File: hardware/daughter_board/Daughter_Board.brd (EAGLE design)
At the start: 65 x 30 mm, 54 parts, among them IC1 LMV358MMX, IC2 LMV358MMX, IC3 ATMEGA2560-16AU, IC5 LMV358MMX, IC8 LMV358MMX, IC9 LMV358MMX, U1 TXB0108DQSR, Y1 CSTCE16M0V53-R0 16MHZ

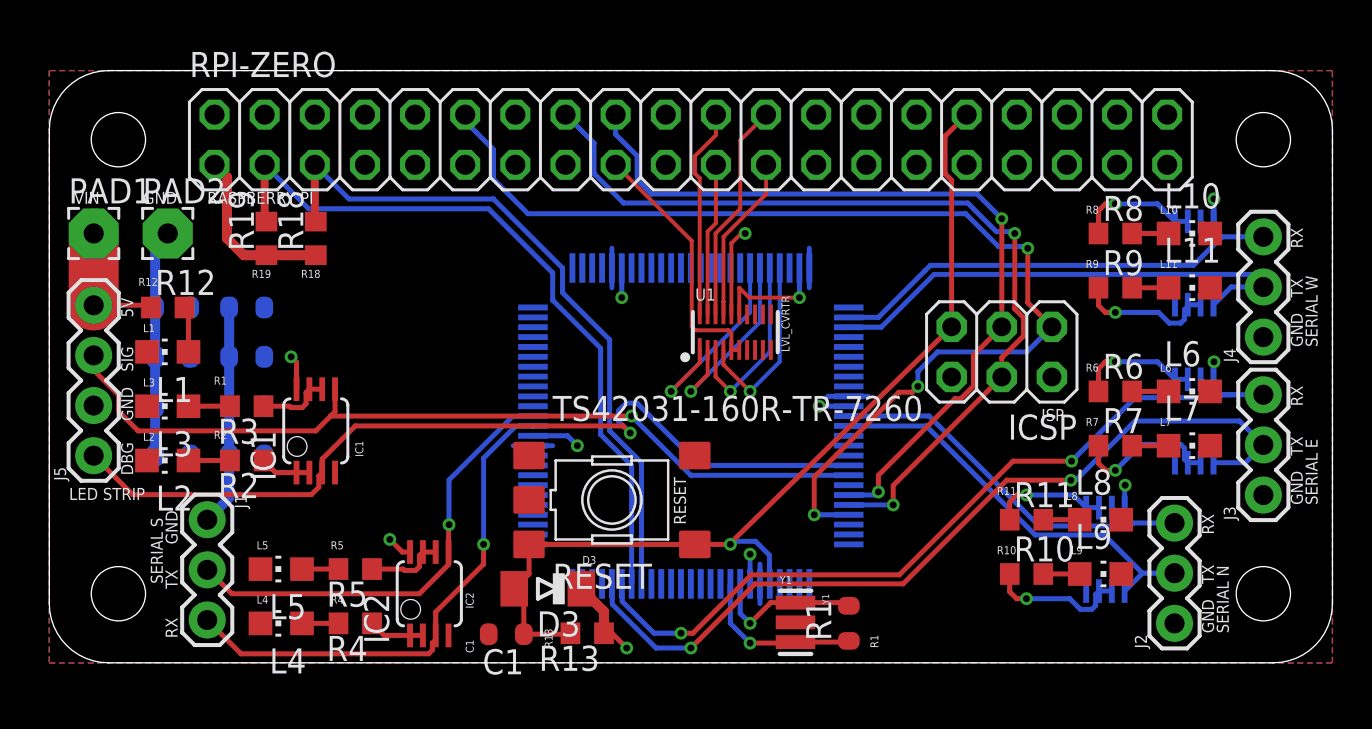
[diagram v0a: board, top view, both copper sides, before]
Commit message: fix issues generated by seeedstudio dru
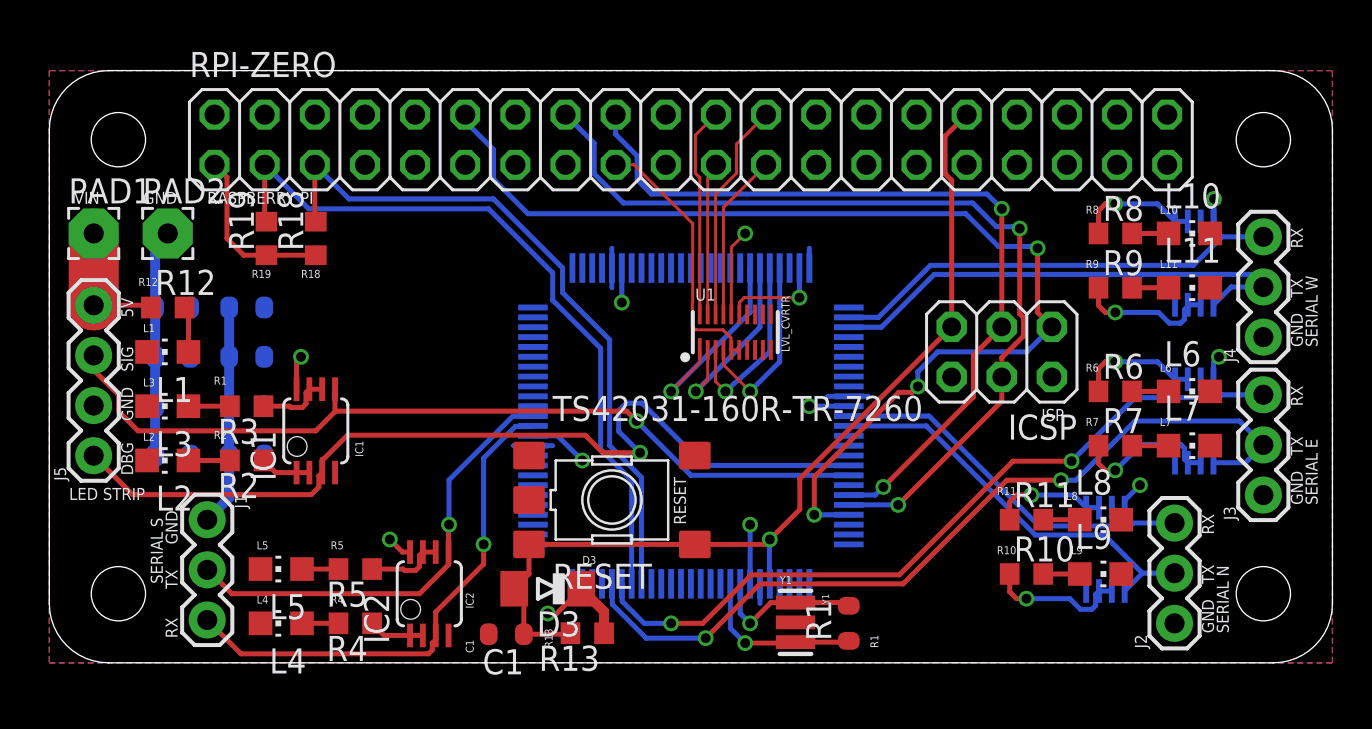
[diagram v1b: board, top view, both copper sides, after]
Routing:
- net GND: track 39.0 -> 41.6 mm
- net RXD1: track 41.5 -> 39.7 mm
- net PH5: track 44.8 -> 46.6 mm
- net +5V: track 28.4 -> 27.0 mm
- net RESET: track 48.5 -> 47.9 mm

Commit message: some DRC fixes
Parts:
- _: value TS42031-160R-TR-7260 -> (none)
- renumbered RESET to _
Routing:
- net +5V: track 27.0 -> 70.3 mm, vias 4 -> 8
- net GND: track 41.6 -> 46.3 mm
- net RESET: track 47.9 -> 49.0 mm

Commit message: export gerber files and create bom
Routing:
- net 3V3_OUT: track 22.4 -> 39.5 mm
- net +5V: track 70.3 -> 78.7 mm
- net GND: track 46.3 -> 50.2 mm
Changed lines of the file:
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@@
 <?xml version="1.0" encoding="utf-8"?>
 <!DOCTYPE eagle SYSTEM "eagle.dtd">
-<eagle version="8.3.2">
+<eagle version="8.4.0">
 <drawing>
 <settings>
@@
 <param name="dpMaxLengthDifference" value="10mm"/>
 <param name="dpGapFactor" value="2.5"/>
-<param name="checkGrid" value="0"/>
-<param name="checkAngle" value="0"/>
 <param name="checkFont" value="1"/>
 <param name="checkRestrict" value="0"/>
+<param name="checkStop" value="0"/>
 <param name="useDiameter" value="13"/>
 <param name="maxErrors" value="50"/>
@@
 <wire x1="32.5944" y1="22.25" x2="29.6144" y2="25.23" width="0.1524" layer="1"/>
 <wire x1="29.6144" y1="25.23" x2="28.69" y2="25.23" width="0.1524" layer="1"/>
-<wire x1="13.5" y1="20.65" x2="28.69" y2="25.23" width="0" layer="19" extent="1-1"/>
+<wire x1="28.69" y1="25.23" x2="24.11" y2="20.65" width="0.254" layer="1"/>
+<wire x1="24.11" y1="20.65" x2="13.5" y2="20.65" width="0.254" layer="1"/>
 </signal>
 <signal name="GPIO4">
@@
 <wire x1="9.96605625" y1="2" x2="8.52605625" y2="3.44" width="0.254" layer="1"/>
 <wire x1="8.52605625" y1="3.44" x2="7.06" y2="3.44" width="0.254" layer="1"/>
-<wire x1="5.361" y1="10.5" x2="4.95" y2="10.25" width="0" layer="19" extent="1-16"/>
+<wire x1="2.2479" y1="13.033" x2="4.95" y2="10.3309" width="0.254" layer="1"/>
+<wire x1="4.95" y1="10.3309" x2="4.95" y2="10.25" width="0.254" layer="1"/>
 </signal>
 <signal name="GPIO17">
@@
 <wire x1="34.55" y1="21.05" x2="35.25" y2="21.75" width="0.1524" layer="1"/>
 <via x="25.25" y="2.5" extent="1-16" drill="0.5"/>
-<wire x1="24.5" y1="11" x2="25.5" y2="11" width="0.3048" layer="16"/>
-<wire x1="25.5" y1="11" x2="25.75" y2="10.75" width="0.3048" layer="16"/>
 <wire x1="23.5" y1="11" x2="24.5" y2="11" width="0.3048" layer="16"/>
 <wire x1="23.5" y1="11" x2="23.25" y2="10.75" width="0.3048" layer="16"/>
@@
 <wire x1="28.5" y1="8.25" x2="31" y2="8.25" width="0.508" layer="1"/>
 <via x="31" y="8.25" extent="1-16" drill="0.5"/>
-<wire x1="36" y1="4" x2="36" y2="7.75" width="0.254" layer="16"/>
-<wire x1="25.5" y1="11" x2="25.5" y2="10.866975" width="0.254" layer="16"/>
-<wire x1="25.5" y1="10.866975" x2="25.5802" y2="10.786775" width="0.254" layer="16"/>
-<wire x1="25.5802" y1="10.786775" x2="25.5802" y2="10.6698" width="0.254" layer="16"/>
-<wire x1="25.5802" y1="10.6698" x2="26" y2="10.25" width="0.254" layer="16"/>
+<wire x1="36" y1="7.75" x2="36" y2="4" width="0.254" layer="16"/>
 <wire x1="28.5" y1="20" x2="28.5" y2="21.5" width="0.254" layer="16"/>
 <wire x1="5.15" y1="18" x2="2.3609" y2="18" width="0.508" layer="1"/>
@@
 <wire x1="48.6404" y1="3.6060625" x2="49.1439375" y2="4.1096" width="0.508" layer="16"/>
 <wire x1="58.5" y1="3.25" x2="58.397" y2="3.147" width="0.508" layer="16"/>
-<wire x1="52.1332125" y1="3.638" x2="52.42" y2="3.638" width="0.508" layer="16"/>
 <wire x1="58.397" y1="3.147" x2="58.397" y2="1.4213375" width="0.508" layer="16"/>
 <wire x1="49.1439375" y1="4.1096" x2="51.6616125" y2="4.1096" width="0.508" layer="16"/>
@@
 <wire x1="57.5786625" y1="0.603" x2="50.9313375" y2="0.603" width="0.508" layer="16"/>
 <wire x1="50.9313375" y1="0.603" x2="48.6404" y2="2.8939375" width="0.508" layer="16"/>
-<wire x1="52.524" y1="3.638" x2="52.42" y2="3.638" width="0" layer="19" extent="16-16"/>
+<wire x1="24.5" y1="11" x2="25.60341875" y2="11" width="0.254" layer="16"/>
+<wire x1="26.69654375" y1="9.5174" x2="27.2326" y2="9.5174" width="0.254" layer="16"/>
+<wire x1="27.2326" y1="9.5174" x2="28.5" y2="8.25" width="0.254" layer="16"/>
+<wire x1="25.60341875" y1="11" x2="25.60341875" y2="10.610525" width="0.254" layer="16"/>
+<wire x1="25.60341875" y1="10.610525" x2="26.69654375" y2="9.5174" width="0.254" layer="16"/>
+<wire x1="31" y1="8.25" x2="35.5" y2="8.25" width="0.254" layer="16"/>
+<wire x1="35.5" y1="8.25" x2="36" y2="7.75" width="0.254" layer="16"/>
+<wire x1="52.1332125" y1="3.638" x2="52.524" y2="3.638" width="0.254" layer="16"/>
 </signal>
 <signal name="5-GND">
@@
 <contactref element="IC5" pad="7"/>
 <contactref element="R7" pad="1"/>
-<wire x1="58.324" y1="10.138" x2="57.674" y2="10.138" width="0.254" layer="16"/>
-<wire x1="57.5042" y1="10.874775" x2="57.310775" y2="11.0682" width="0.254" layer="16"/>
-<wire x1="57.674" y1="10.138" x2="57.5042" y2="10.3078" width="0.254" layer="16"/>
-<wire x1="57.5042" y1="10.3078" x2="57.5042" y2="10.874775" width="0.254" layer="16"/>
-<wire x1="57.310775" y1="11.0682" x2="55.3182" y2="11.0682" width="0.254" layer="16"/>
-<wire x1="55.3182" y1="11.0682" x2="54" y2="9.75" width="0.254" layer="16"/>
+<wire x1="57.75" y1="10.138" x2="58.324" y2="10.138" width="0.254" layer="16"/>
+<wire x1="57.75" y1="10.138" x2="57.674" y2="10.138" width="0.254" layer="16"/>
+<wire x1="54" y1="9.75" x2="55.3182" y2="11.0682" width="0.254" layer="16"/>
 <via x="54" y="9.75" extent="1-16" drill="0.5"/>
 <wire x1="53.5" y1="9.75" x2="54" y2="9.75" width="0.254" layer="1"/>
 <wire x1="53.15" y1="11" x2="53.15" y2="10.1" width="0.254" layer="1"/>
 <wire x1="53.15" y1="10.1" x2="53.5" y2="9.75" width="0.254" layer="1"/>
+<wire x1="55.3182" y1="11.0682" x2="57.4318" y2="11.0682" width="0.254" layer="16"/>
+<wire x1="57.4318" y1="11.0682" x2="57.75" y2="10.75" width="0.254" layer="16"/>
+<wire x1="57.75" y1="10.75" x2="57.75" y2="10.138" width="0.254" layer="16"/>
 </signal>
 <signal name="N$7">

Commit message: Daughter Board v1
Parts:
- removed _: (no value), SmartPrj:TS42
- added S1: MOMENTARY-SWITCH-SPST-SMD-5.2-REDUNDANT, SparkFun-Switches:TACTILE_SWITCH_SMD_5.2MM
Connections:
- removed net 5-GND: _.5
- net GND: now also S1.1, S1.2; no longer _.1, _.2
- net RESET: now also S1.3, S1.4; no longer _.3, _.4
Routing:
- net RESET: track 49.0 -> 52.3 mm
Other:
- board text added: "Authors: Rauhul Varma Naren Dasan"
- board text added: "TWILIGHT Ver. 0.1 ACM@UIUC"
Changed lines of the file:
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@@
 <layer number="21" name="tPlace" color="7" fill="1" visible="yes" active="yes"/>
 <layer number="22" name="bPlace" color="7" fill="1" visible="yes" active="yes"/>
-<layer number="23" name="tOrigins" color="15" fill="1" visible="no" active="yes"/>
+<layer number="23" name="tOrigins" color="15" fill="1" visible="yes" active="yes"/>
 <layer number="24" name="bOrigins" color="15" fill="1" visible="no" active="yes"/>
 <layer number="25" name="tNames" color="7" fill="1" visible="no" active="yes"/>
@@
 <text x="51.5" y="7" size="0.4064" layer="22" font="vector" rot="MR270">IC8</text>
 <text x="23.25" y="18" size="0.4064" layer="22" font="vector" rot="MR270">IC3</text>
+<text x="16.5" y="16.5" size="0.8128" layer="21" font="vector">TWILIGHT
+Ver. 0.1
+ACM@UIUC </text>
+<text x="16.5" y="13.25" size="0.6096" layer="21" font="vector">Authors:
+Rauhul Varma
+Naren Dasan</text>
 </plain>
 <attributes>
@@
 <element name="Y1" library="SmartPrj" package="RESONATOR" value="CSTCE16M0V53-R0 16MHZ" x="37.8" y="2.05" rot="R270"/>
 <element name="R1" library="SmartPrj" package="R0603-ROUND" value="1M" x="40.5" y="2" rot="R90"/>
-<element name="_" library="SmartPrj" package="TS42" value="" x="28.5" y="8.25"/>
 <element name="D3" library="diode" package="MINIMELF" value="CD1206-S01575" x="25.25" y="3.75" rot="R180"/>
 <element name="IC1" library="linear" library_urn="urn:adsk.eagle:library:262" package="MSOP08" package3d_urn="urn:adsk.eagle:package:16453/1" value="LMV358MMX" x="13.5" y="11.75"/>
@@
 <attribute name="PROD_ID" value="IC-12292" x="34.75" y="16.75" size="1.778" layer="27" display="off"/>
 </element>
+<element name="S1" library="SparkFun-Switches" library_urn="urn:adsk.eagle:library:535" package="TACTILE_SWITCH_SMD_5.2MM" package3d_urn="urn:adsk.eagle:package:40167/1" value="MOMENTARY-SWITCH-SPST-SMD-5.2-REDUNDANT" x="29.5" y="7.25" rot="R180">
+<attribute name="PROD_ID" value="SWCH-08247" x="29.5" y="7.25" size="1.778" layer="27" rot="R180" display="off"/>
+<attribute name="SF_SKU" value="COM-08720" x="29.5" y="7.25" size="1.778" layer="27" rot="R180" display="off"/>
+</element>
 </elements>
 <signals>
@@
 <contactref element="IC3" pad="11"/>
 <contactref element="L1" pad="C"/>
-<contactref element="_" pad="1"/>
-<contactref element="_" pad="2"/>
 <contactref element="C4" pad="2"/>
 <contactref element="C5" pad="2"/>
@@
 <wire x1="2.2479" y1="13.033" x2="4.95" y2="10.3309" width="0.254" layer="1"/>
 <wire x1="4.95" y1="10.3309" x2="4.95" y2="10.25" width="0.254" layer="1"/>
+<contactref element="S1" pad="1"/>
+<contactref element="S1" pad="2"/>
 </signal>
 <signal name="GPIO17">
@@
 <wire x1="23.5" y1="11" x2="23.25" y2="10.75" width="0.3048" layer="16"/>
 <wire x1="39.25" y1="13.5" x2="40.5" y2="13.5" width="0.3048" layer="16"/>
-<wire x1="42" y1="13.5" x2="41.75" y2="13.5" width="0.3048" layer="16"/>
 <via x="43.5" y="16.75" extent="1-16" drill="0.5"/>
 <wire x1="43.5" y1="16.75" x2="43.5" y2="17.75" width="0.508" layer="1"/>
 <wire x1="43.5" y1="17.75" x2="42" y2="19.25" width="0.508" layer="1"/>
 <via x="42" y="19.25" extent="1-16" drill="0.5"/>
-<wire x1="40.5" y1="13.5" x2="41.75" y2="13.5" width="0.3048" layer="16"/>
 <wire x1="41.75" y1="13.5" x2="42.5" y2="14.25" width="0.3048" layer="16"/>
 <wire x1="42.5" y1="14.25" x2="42.5" y2="15.75" width="0.3048" layer="16"/>
@@
 <wire x1="57.5786625" y1="0.603" x2="50.9313375" y2="0.603" width="0.508" layer="16"/>
 <wire x1="50.9313375" y1="0.603" x2="48.6404" y2="2.8939375" width="0.508" layer="16"/>
-<wire x1="24.5" y1="11" x2="25.60341875" y2="11" width="0.254" layer="16"/>
 <wire x1="26.69654375" y1="9.5174" x2="27.2326" y2="9.5174" width="0.254" layer="16"/>
 <wire x1="27.2326" y1="9.5174" x2="28.5" y2="8.25" width="0.254" layer="16"/>
-<wire x1="25.60341875" y1="11" x2="25.60341875" y2="10.610525" width="0.254" layer="16"/>
-<wire x1="25.60341875" y1="10.610525" x2="26.69654375" y2="9.5174" width="0.254" layer="16"/>
 <wire x1="31" y1="8.25" x2="35.5" y2="8.25" width="0.254" layer="16"/>
 <wire x1="35.5" y1="8.25" x2="36" y2="7.75" width="0.254" layer="16"/>
 <wire x1="52.1332125" y1="3.638" x2="52.524" y2="3.638" width="0.254" layer="16"/>
-</signal>
-<signal name="5-GND">
-<contactref element="_" pad="5"/>
+<wire x1="26.2674" y1="10.2326" x2="25.5" y2="11" width="0.254" layer="16"/>
+<wire x1="24.5" y1="11" x2="25.5" y2="11" width="0.254" layer="16"/>
+<wire x1="26.2674" y1="10.2326" x2="26.2674" y2="9.94654375" width="0.254" layer="16"/>
+<wire x1="26.2674" y1="9.94654375" x2="26.69654375" y2="9.5174" width="0.254" layer="16"/>
+<wire x1="40.5" y1="13.5" x2="41.75" y2="13.5" width="0.3048" layer="16"/>
 </signal>
 <signal name="RESET">
-<contactref element="_" pad="4"/>
-<contactref element="_" pad="3"/>
 <contactref element="IC3" pad="30"/>
 <contactref element="C1" pad="1"/>
@@
 <contactref element="ICSP" pad="5"/>
 <contactref element="R13" pad="2"/>
-<wire x1="32.7" y1="6" x2="24.3" y2="6" width="0.254" layer="1"/>
 <wire x1="36.5" y1="4" x2="36.4802" y2="4.0198" width="0.254" layer="16"/>
 <wire x1="26.35" y1="1.45" x2="24.039" y2="1.45" width="0.254" layer="1"/>
@@
 <wire x1="24.039" y1="3.261" x2="23.55" y2="3.75" width="0.254" layer="1"/>
 <wire x1="23.55" y1="3.75" x2="24.3" y2="4.5" width="0.254" layer="1"/>
-<wire x1="24.3" y1="4.5" x2="24.3" y2="6" width="0.254" layer="1"/>
 <contactref element="RPI-ZERO" pad="32"/>
 <wire x1="45.71" y1="17.02" x2="45.71" y2="24.44539375" width="0.254" layer="1"/>
@@
 <wire x1="45.3778" y1="26.6778" x2="46.47" y2="27.77" width="0.254" layer="1"/>
 <via x="37.25" y="7" extent="1-16" drill="0.5"/>
-<wire x1="36.25" y1="6" x2="37.25" y2="7" width="0.254" layer="1"/>
-<wire x1="36.25" y1="6" x2="32.7" y2="6" width="0.254" layer="1"/>
 <wire x1="45.43605" y1="16.74605625" x2="45.43605625" y2="16.74605625" width="0.254" layer="1"/>
 <wire x1="45.43605625" y1="16.74605625" x2="45.71" y2="17.02" width="0.254" layer="1"/>
@@
 <wire x1="37" y1="6.75" x2="37.25" y2="7" width="0.254" layer="16"/>
 <wire x1="36.4802" y1="4.0198" x2="36.4802" y2="5.7302" width="0.254" layer="16"/>
+<contactref element="S1" pad="3"/>
+<contactref element="S1" pad="4"/>
+<wire x1="23.55" y1="3.75" x2="25.6138" y2="5.8138" width="0.254" layer="1"/>
+<wire x1="25.6138" y1="5.8138" x2="25.6138" y2="5.862775" width="0.254" layer="1"/>
+<wire x1="26.706" y1="6.954975" x2="26.706" y2="9.155" width="0.254" layer="1"/>
+<wire x1="25.6138" y1="5.862775" x2="26.706" y2="6.954975" width="0.254" layer="1"/>
+<wire x1="26.706" y1="9.155" x2="32.294" y2="9.155" width="0.254" layer="1"/>
+<wire x1="32.294" y1="9.155" x2="35.095" y2="9.155" width="0.254" layer="1"/>
+<wire x1="35.095" y1="9.155" x2="37.25" y2="7" width="0.254" layer="1"/>
 </signal>
 <signal name="N$3">
@@
 </drawing>
 <compatibility>
+<note version="6.3" minversion="6.2.2" severity="warning">
+Since Version 6.2.2 text objects can contain more than one line,
+which will not be processed correctly with this version.
+</note>
 <note version="8.2" severity="warning">
 Since Version 8.2, EAGLE supports online libraries. The ids

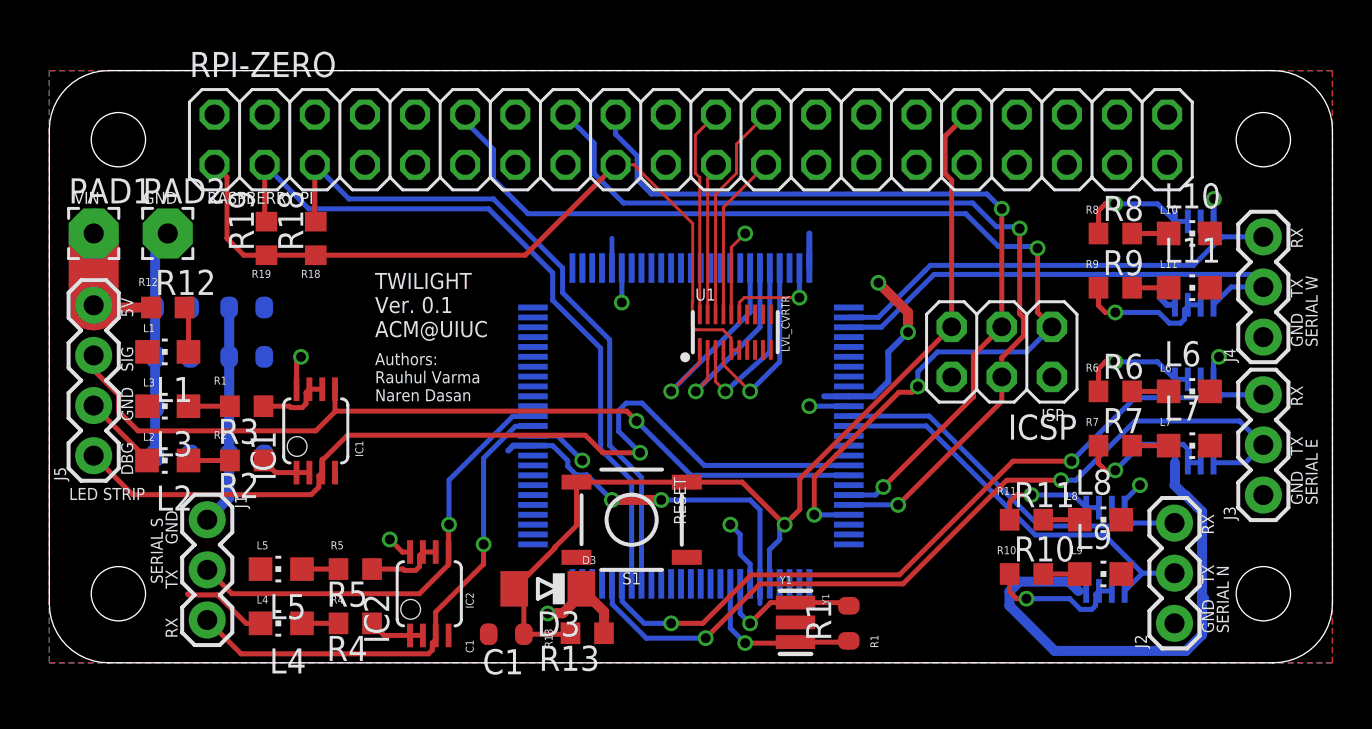
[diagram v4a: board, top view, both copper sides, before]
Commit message: update silkscreen and export gerber files
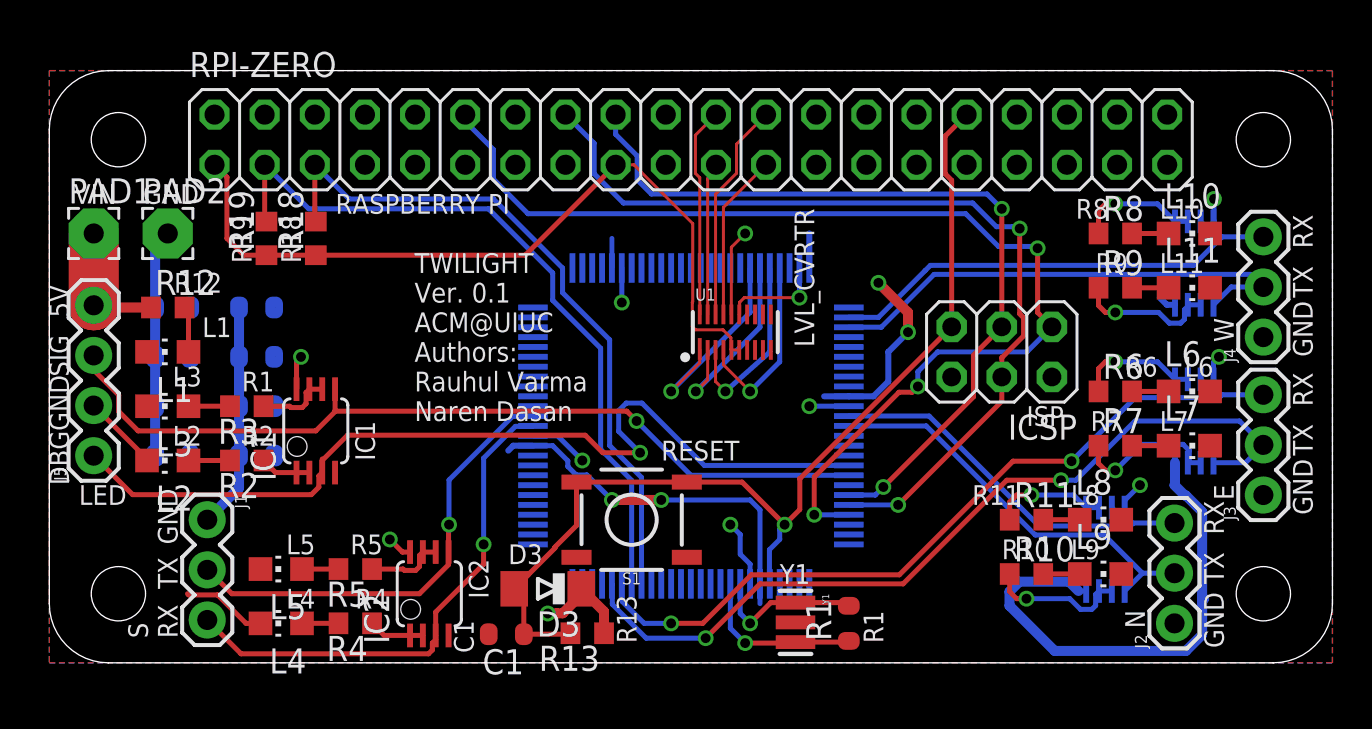
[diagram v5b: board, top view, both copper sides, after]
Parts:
- moved C16 0.50 mm to (10.5, 15.5)
- moved C17 0.50 mm to (10.5, 18.0)
- moved C18 0.50 mm to (10.5, 13.0)
- moved C2 0.50 mm to (10.5, 10.5)
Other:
- board text added: "C18"
- board text added: "E"
- board text added: "LED"
- board text added: "N"
- board text added: "S"
- board text added: "W"
- board text removed: "LED STRIP"
- board text removed: "SERIAL E"
- board text removed: "SERIAL N"
- board text removed: "SERIAL S"
- board text removed: "SERIAL W"
